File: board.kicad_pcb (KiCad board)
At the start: 4 copper layers, 90 x 80 mm, 13 parts, among them J1 chip_inst_mem_o, J10 chip_data_mem_o_1, J11 base, J12 power, J2 chip_data_mem_o_1, J3 data_mem_i, J4 chip_data_mem_o_1, J5 data_mem_i, J6 chip_data_mem_o_3, J7 inst_mem_i, J8 inst_mem_i, J9 chip_data_mem_o_1, U1 BERYL-MBLite

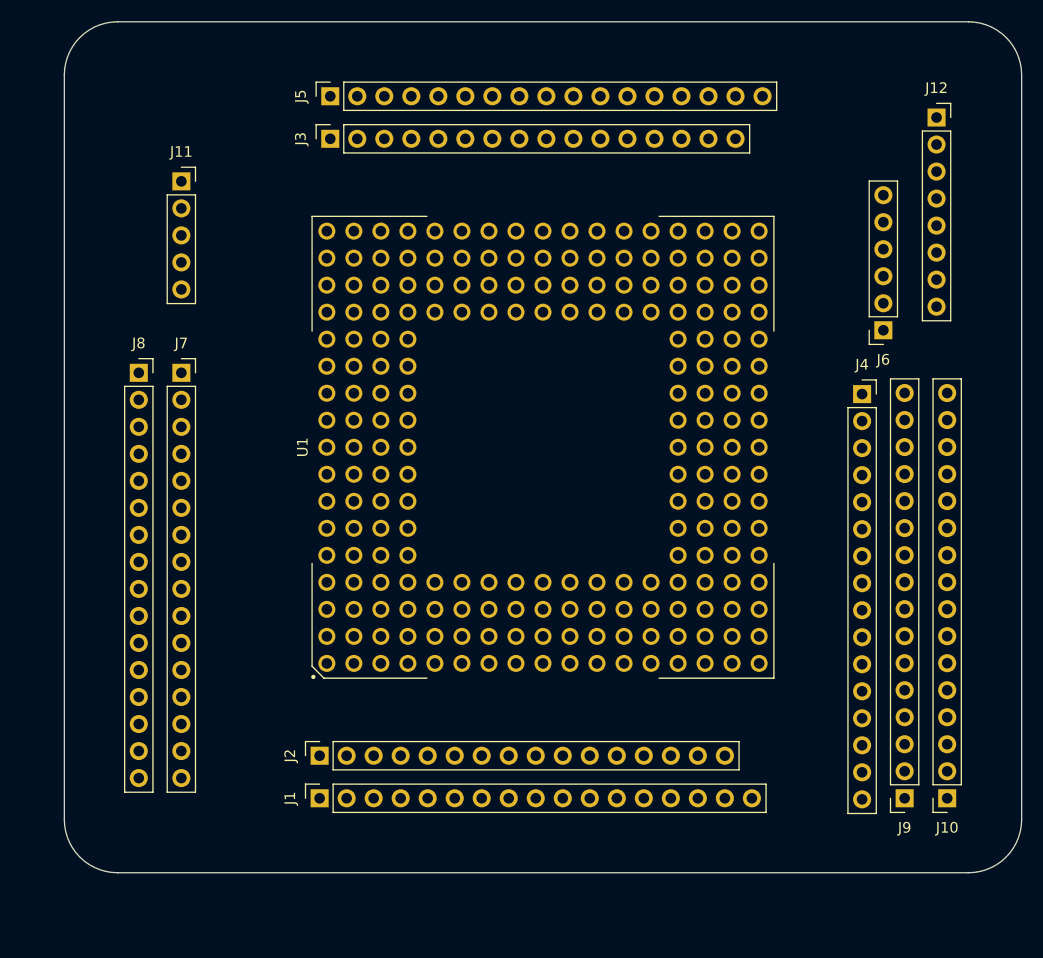
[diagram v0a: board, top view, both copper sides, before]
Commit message: Change headers to SMD and add decoupling capacitors
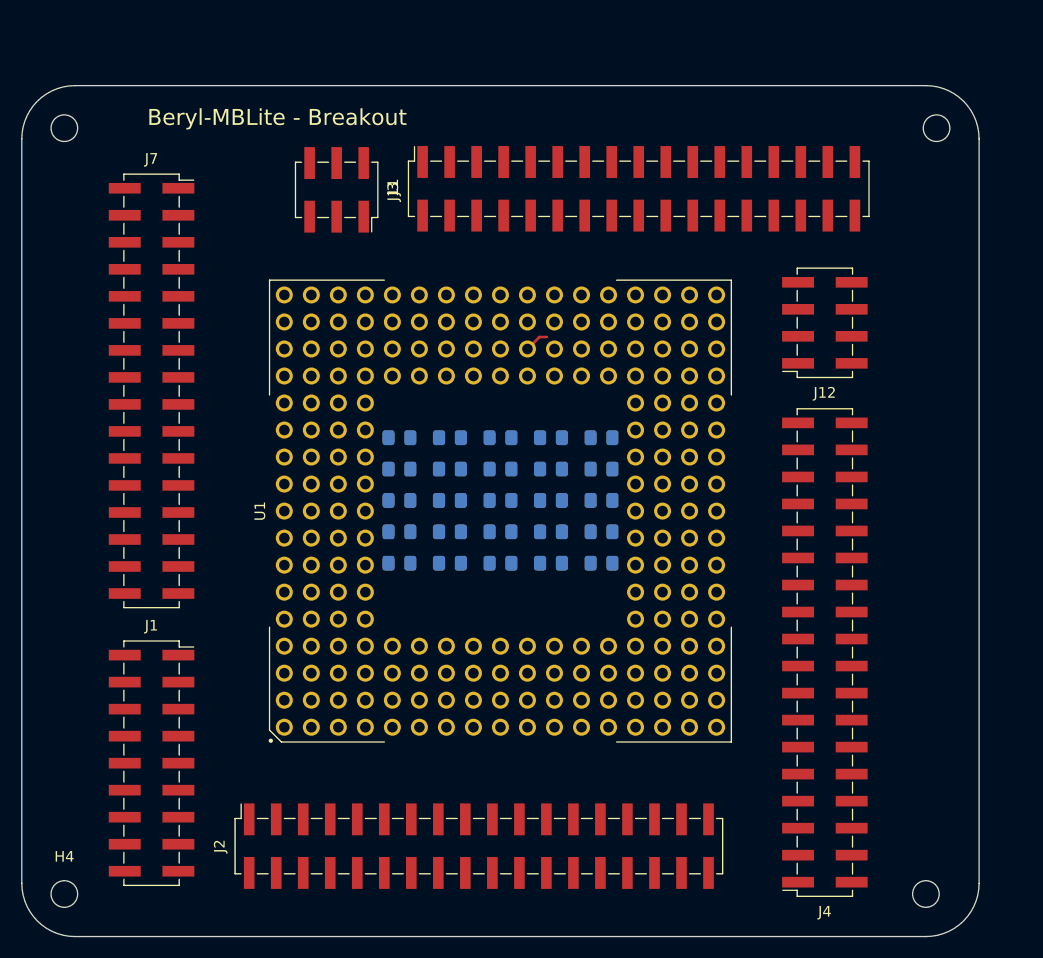
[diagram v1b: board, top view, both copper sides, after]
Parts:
- removed J10, J9: chip_data_mem_o_1, Connector_PinSocket_2.54mm:PinSocket_1x16_P2.54mm_Vertical
- removed J5: data_mem_i, Connector_PinSocket_2.54mm:PinSocket_1x17_P2.54mm_Vertical
- removed J6: chip_data_mem_o_3, Connector_PinSocket_2.54mm:PinSocket_1x06_P2.54mm_Vertical
- removed J8: inst_mem_i, Connector_PinSocket_2.54mm:PinSocket_1x16_P2.54mm_Vertical
- added C1: 100n, Capacitor_SMD:C_0805_2012Metric_Pad1.15x1.40mm_HandSolder, B.Cu at (151.0, 95.0)
- added C10: 100n, Capacitor_SMD:C_0805_2012Metric_Pad1.15x1.40mm_HandSolder, B.Cu at (141.5, 89.1)
- added C11: 100n, Capacitor_SMD:C_0805_2012Metric_Pad1.15x1.40mm_HandSolder, B.Cu at (155.8, 100.9)
- added C12: 100n, Capacitor_SMD:C_0805_2012Metric_Pad1.15x1.40mm_HandSolder, B.Cu at (146.2, 92.0)
- added C13: 100n, Capacitor_SMD:C_0805_2012Metric_Pad1.15x1.40mm_HandSolder, B.Cu at (155.8, 98.0)
- added C14: 100n, Capacitor_SMD:C_0805_2012Metric_Pad1.15x1.40mm_HandSolder, B.Cu at (141.5, 100.9)
- added C15: 100n, Capacitor_SMD:C_0805_2012Metric_Pad1.15x1.40mm_HandSolder, B.Cu at (146.2, 89.1)
- added C16: 100n, Capacitor_SMD:C_0805_2012Metric_Pad1.15x1.40mm_HandSolder, B.Cu at (160.5, 100.9)
- added C17: 100n, Capacitor_SMD:C_0805_2012Metric_Pad1.15x1.40mm_HandSolder, B.Cu at (151.0, 92.0)
- added C18: 100n, Capacitor_SMD:C_0805_2012Metric_Pad1.15x1.40mm_HandSolder, B.Cu at (155.8, 95.0)
- added C19: 100n, Capacitor_SMD:C_0805_2012Metric_Pad1.15x1.40mm_HandSolder, B.Cu at (160.5, 98.0)
- added C2: 100n, Capacitor_SMD:C_0805_2012Metric_Pad1.15x1.40mm_HandSolder, B.Cu at (141.5, 98.0)
- added C20: 100n, Capacitor_SMD:C_0805_2012Metric_Pad1.15x1.40mm_HandSolder, B.Cu at (151.0, 89.1)
- added C21: 100n, Capacitor_SMD:C_0805_2012Metric_Pad1.15x1.40mm_HandSolder, B.Cu at (155.8, 92.0)
- added C22: 100n, Capacitor_SMD:C_0805_2012Metric_Pad1.15x1.40mm_HandSolder, B.Cu at (160.5, 95.0)
- added C23: 100n, Capacitor_SMD:C_0805_2012Metric_Pad1.15x1.40mm_HandSolder, B.Cu at (155.8, 89.1)
- added C24: 100n, Capacitor_SMD:C_0805_2012Metric_Pad1.15x1.40mm_HandSolder, B.Cu at (160.5, 92.0)
- added C25: 100n, Capacitor_SMD:C_0805_2012Metric_Pad1.15x1.40mm_HandSolder, B.Cu at (160.5, 89.1)
- added C3: 100n, Capacitor_SMD:C_0805_2012Metric_Pad1.15x1.40mm_HandSolder, B.Cu at (146.2, 100.9)
- added C4: 100n, Capacitor_SMD:C_0805_2012Metric_Pad1.15x1.40mm_HandSolder, B.Cu at (141.5, 95.0)
- added C5: 100n, Capacitor_SMD:C_0805_2012Metric_Pad1.15x1.40mm_HandSolder, B.Cu at (146.2, 98.0)
- added C6: 100n, Capacitor_SMD:C_0805_2012Metric_Pad1.15x1.40mm_HandSolder, B.Cu at (151.0, 100.9)
- added C7: 100n, Capacitor_SMD:C_0805_2012Metric_Pad1.15x1.40mm_HandSolder, B.Cu at (141.5, 92.0)
- added C8: 100n, Capacitor_SMD:C_0805_2012Metric_Pad1.15x1.40mm_HandSolder, B.Cu at (146.2, 95.0)
- added C9: 100n, Capacitor_SMD:C_0805_2012Metric_Pad1.15x1.40mm_HandSolder, B.Cu at (151.0, 98.0)
- added H1: MountingHole, MountingHole:MountingHole_2.5mm, F.Cu at (110.0, 60.0)
- added H2: MountingHole, MountingHole:MountingHole_2.5mm, F.Cu at (192.0, 60.0)
- added H3: MountingHole, MountingHole:MountingHole_2.5mm, F.Cu at (191.0, 132.0)
- added H4: MountingHole, MountingHole:MountingHole_2.5mm, F.Cu at (110.0, 132.0)
- J1: footprint Connector_PinSocket_2.54mm:PinSocket_1x17_P2.54mm_Vertical -> Connector_PinSocket_2.54mm:PinSocket_2x09_P2.54mm_Vertical_SMD
- J11: footprint Connector_PinSocket_2.54mm:PinSocket_1x05_P2.54mm_Vertical -> Connector_PinSocket_2.54mm:PinSocket_2x03_P2.54mm_Vertical_SMD
- J12: footprint Connector_PinSocket_2.54mm:PinSocket_1x08_P2.54mm_Vertical -> Connector_PinSocket_2.54mm:PinSocket_2x04_P2.54mm_Vertical_SMD
- J2, J4: footprint Connector_PinSocket_2.54mm:PinSocket_1x16_P2.54mm_Vertical -> Connector_PinSocket_2.54mm:PinSocket_2x18_P2.54mm_Vertical_SMD
- J3: footprint Connector_PinSocket_2.54mm:PinSocket_1x16_P2.54mm_Vertical -> Connector_PinSocket_2.54mm:PinSocket_2x17_P2.54mm_Vertical_SMD
- J7: footprint Connector_PinSocket_2.54mm:PinSocket_1x16_P2.54mm_Vertical -> Connector_PinSocket_2.54mm:PinSocket_2x16_P2.54mm_Vertical_SMD
- moved J3 29.4 mm to (164.0, 65.7)
- moved J4 24.6 mm to (181.5, 109.3), turned to 180 degrees
- moved J12 22.0 mm to (181.5, 78.3), turned to 180 degrees
- moved J2 17.2 mm to (149.0, 127.5)
- moved J1 16.1 mm to (118.2, 119.7), turned to 0 degrees
- moved J11 14.6 mm to (135.6, 65.8), turned to 270 degrees
- moved U1 7.21 mm to (151.0, 96.0)
- moved J7 3.28 mm to (118.2, 84.7)
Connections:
- U1 pad 1: Net-(J8-Pad7) -> Net-(J7-Pad10)
- U1 pad 10: Net-(J7-Pad1) -> Net-(J7-Pad17)
- U1 pad 100: Net-(J4-Pad5) -> Net-(J2-Pad21)
- U1 pad 101: Net-(J4-Pad4) -> Net-(J2-Pad20)
- U1 pad 102: Net-(J4-Pad3) -> Net-(J2-Pad19)
- U1 pad 103: Net-(J4-Pad2) -> Net-(J2-Pad18)
- U1 pad 104: Net-(J4-Pad1) -> Net-(J2-Pad17)
- U1 pad 107: Net-(J9-Pad5) -> Net-(J4-Pad2)
- U1 pad 108: Net-(J9-Pad6) -> Net-(J4-Pad3)
- U1 pad 109: Net-(J9-Pad7) -> Net-(J4-Pad4)
- U1 pad 11: Net-(J7-Pad2) -> Net-(J7-Pad18)
- U1 pad 110: Net-(J9-Pad8) -> Net-(J4-Pad5)
- U1 pad 111: Net-(J9-Pad9) -> Net-(J4-Pad6)
- U1 pad 112: Net-(J9-Pad10) -> Net-(J4-Pad7)
- U1 pad 113: Net-(J9-Pad11) -> Net-(J4-Pad8)
- U1 pad 114: Net-(J9-Pad12) -> Net-(J4-Pad9)
- U1 pad 115: Net-(J9-Pad13) -> Net-(J4-Pad10)
- U1 pad 118: Net-(J9-Pad14) -> Net-(J4-Pad11)
- U1 pad 119: Net-(J9-Pad15) -> Net-(J4-Pad12)
- U1 pad 12: Net-(J7-Pad3) -> Net-(J7-Pad19)
- U1 pad 122: Net-(J9-Pad16) -> Net-(J4-Pad13)
- U1 pad 123: Net-(J10-Pad1) -> Net-(J4-Pad14)
- U1 pad 124: Net-(J10-Pad2) -> Net-(J4-Pad15)
- U1 pad 125: Net-(J10-Pad3) -> Net-(J4-Pad16)
- U1 pad 126: Net-(J10-Pad4) -> Net-(J4-Pad17)
- U1 pad 127: Net-(J10-Pad5) -> Net-(J4-Pad18)
- U1 pad 128: Net-(J10-Pad6) -> Net-(J4-Pad19)
- U1 pad 129: Net-(J10-Pad7) -> Net-(J4-Pad20)
- U1 pad 13: Net-(J7-Pad4) -> Net-(J7-Pad20)
- U1 pad 130: Net-(J10-Pad8) -> Net-(J4-Pad21)
- U1 pad 131: Net-(J10-Pad9) -> Net-(J4-Pad22)
- U1 pad 132: Net-(J10-Pad10) -> Net-(J4-Pad23)
- U1 pad 133: Net-(J10-Pad11) -> Net-(J4-Pad24)
- U1 pad 136: Net-(J10-Pad12) -> Net-(J4-Pad25)
- U1 pad 139: Net-(J10-Pad13) -> Net-(J4-Pad26)
- U1 pad 14: Net-(J7-Pad5) -> Net-(J7-Pad21)
- U1 pad 140: Net-(J10-Pad14) -> Net-(J4-Pad27)
- U1 pad 141: Net-(J10-Pad15) -> Net-(J4-Pad28)
- U1 pad 142: Net-(J10-Pad16) -> Net-(J4-Pad29)
- U1 pad 143: Net-(J6-Pad1) -> Net-(J4-Pad30)
- U1 pad 144: Net-(J6-Pad2) -> Net-(J4-Pad31)
- U1 pad 145: Net-(J6-Pad3) -> Net-(J4-Pad32)
- U1 pad 146: Net-(J6-Pad4) -> Net-(J4-Pad33)
- U1 pad 147: Net-(J6-Pad5) -> Net-(J4-Pad34)
- U1 pad 148: Net-(J6-Pad6) -> Net-(J4-Pad35)
- U1 pad 15: Net-(J7-Pad6) -> Net-(J7-Pad22)
- U1 pad 153: Net-(J5-Pad17) -> Net-(J3-Pad33)
- U1 pad 154: Net-(J5-Pad16) -> Net-(J3-Pad32)
- U1 pad 155: Net-(J5-Pad15) -> Net-(J3-Pad31)
- U1 pad 156: Net-(J5-Pad14) -> Net-(J3-Pad30)
- U1 pad 157: Net-(J5-Pad13) -> Net-(J3-Pad29)
- U1 pad 158: Net-(J5-Pad12) -> Net-(J3-Pad28)
- U1 pad 159: Net-(J5-Pad11) -> Net-(J3-Pad27)
- U1 pad 160: Net-(J5-Pad10) -> Net-(J3-Pad26)
- U1 pad 163: Net-(J5-Pad9) -> Net-(J3-Pad25)
- U1 pad 164: Net-(J5-Pad8) -> Net-(J3-Pad24)
- U1 pad 165: Net-(J5-Pad7) -> Net-(J3-Pad23)
- U1 pad 166: Net-(J5-Pad6) -> Net-(J3-Pad22)
- U1 pad 167: Net-(J5-Pad5) -> Net-(J3-Pad21)
- U1 pad 168: Net-(J5-Pad4) -> Net-(J3-Pad20)
- U1 pad 169: Net-(J5-Pad3) -> Net-(J3-Pad19)
- U1 pad 170: Net-(J5-Pad2) -> Net-(J3-Pad18)
- U1 pad 171: Net-(J5-Pad1) -> Net-(J3-Pad17)
- U1 pad 18: Net-(J7-Pad7) -> Net-(J7-Pad23)
- U1 pad 19: Net-(J7-Pad8) -> Net-(J7-Pad24)
- U1 pad 192: Net-(J8-Pad16) -> Net-(J7-Pad1)
- U1 pad 193: Net-(J8-Pad15) -> Net-(J7-Pad2)
- U1 pad 2: Net-(J8-Pad6) -> Net-(J7-Pad11)
- U1 pad 20: Net-(J7-Pad9) -> Net-(J7-Pad25)
- U1 pad 202: Net-(J8-Pad14) -> Net-(J7-Pad3)
- U1 pad 203: Net-(J8-Pad13) -> Net-(J7-Pad4)
- U1 pad 204: Net-(J8-Pad12) -> Net-(J7-Pad5)
- U1 pad 205: Net-(J8-Pad11) -> Net-(J7-Pad6)
- U1 pad 206: Net-(J8-Pad10) -> Net-(J7-Pad7)
- U1 pad 207: Net-(J8-Pad9) -> Net-(J7-Pad8)
- U1 pad 208: Net-(J8-Pad8) -> Net-(J7-Pad9)
- U1 pad 21: Net-(J7-Pad10) -> Net-(J7-Pad26)
- U1 pad 22: Net-(J7-Pad11) -> Net-(J7-Pad27)
- U1 pad 23: Net-(J7-Pad12) -> Net-(J7-Pad28)
- U1 pad 24: Net-(J7-Pad13) -> Net-(J7-Pad29)
- U1 pad 27: Net-(J7-Pad14) -> Net-(J7-Pad30)
- U1 pad 28: Net-(J7-Pad15) -> Net-(J7-Pad31)
- U1 pad 29: Net-(J7-Pad16) -> Net-(J7-Pad32)
- U1 pad 3: Net-(J8-Pad5) -> Net-(J7-Pad12)
- U1 pad 4: Net-(J8-Pad4) -> Net-(J7-Pad13)
- U1 pad 5: Net-(J8-Pad3) -> Net-(J7-Pad14)
- U1 pad 6: Net-(J8-Pad2) -> Net-(J7-Pad15)
- U1 pad 7: Net-(J8-Pad1) -> Net-(J7-Pad16)
- U1 pad 79: Net-(J9-Pad4) -> Net-(J4-Pad1)
- U1 pad 80: Net-(J9-Pad3) -> Net-(J2-Pad35)
- U1 pad 81: Net-(J9-Pad2) -> Net-(J2-Pad34)
- U1 pad 82: Net-(J9-Pad1) -> Net-(J2-Pad33)
- U1 pad 83: Net-(J4-Pad16) -> Net-(J2-Pad32)
- U1 pad 84: Net-(J4-Pad15) -> Net-(J2-Pad31)
- U1 pad 85: Net-(J4-Pad14) -> Net-(J2-Pad30)
- U1 pad 88: Net-(J4-Pad13) -> Net-(J2-Pad29)
- U1 pad 89: Net-(J4-Pad12) -> Net-(J2-Pad28)
- U1 pad 90: Net-(J4-Pad11) -> Net-(J2-Pad27)
- U1 pad 93: Net-(J4-Pad10) -> Net-(J2-Pad26)
- U1 pad 94: Net-(J4-Pad9) -> Net-(J2-Pad25)
- U1 pad 95: Net-(J4-Pad8) -> Net-(J2-Pad24)
- U1 pad 96: Net-(J4-Pad7) -> Net-(J2-Pad23)
- U1 pad 99: Net-(J4-Pad6) -> Net-(J2-Pad22)
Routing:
- net +1V8: track 0.00 -> 154.9 mm
- net +3V3: track 0.00 -> 133.3 mm
- net GND: track 0.00 -> 7.62 mm
- net Net-(J3-Pad12): track 0.00 -> 2.29 mm
- net Net-(J3-Pad14): track 0.00 -> 0.69 mm
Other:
- board text added: "Beryl-MBLite - Breakout"
- board text added: "Grupo de Apoio ao Projeto de Hardware GAPH - PUCRS - xx.xx.xx"

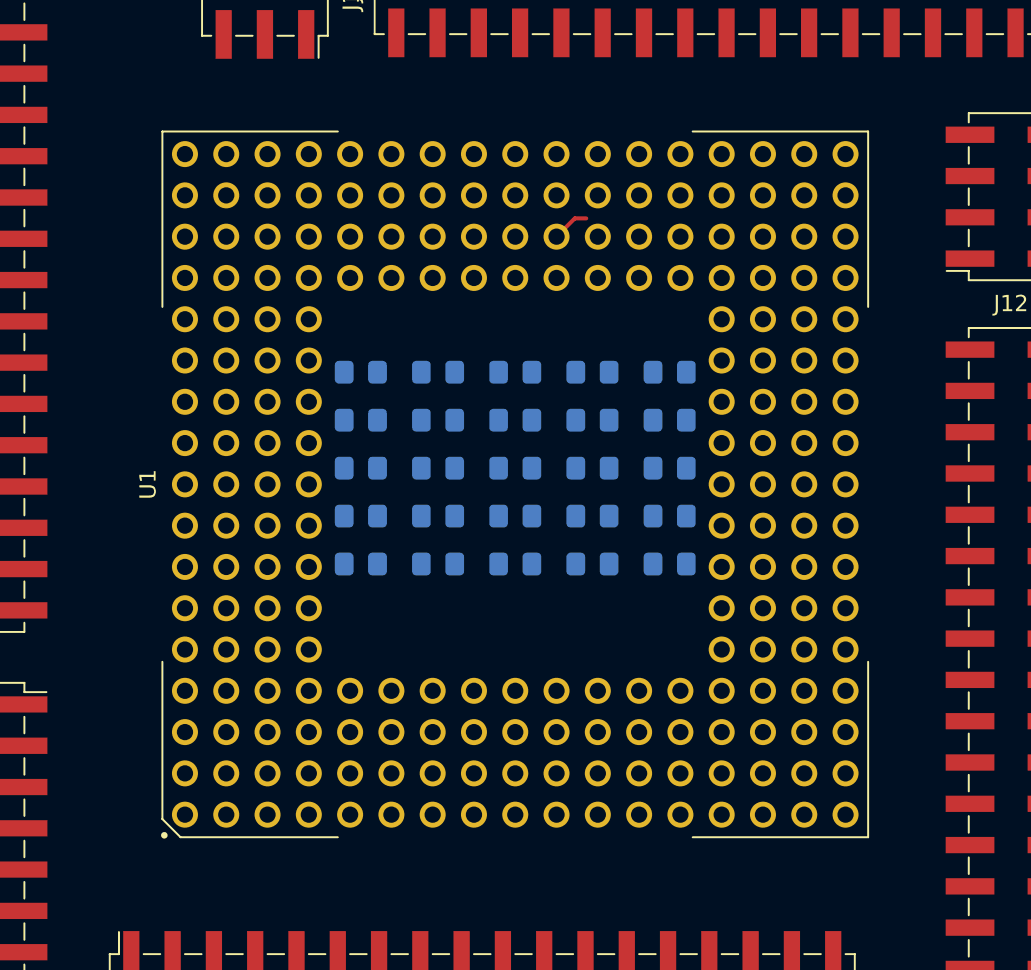
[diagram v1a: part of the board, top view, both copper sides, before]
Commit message: Improve capacitors placement
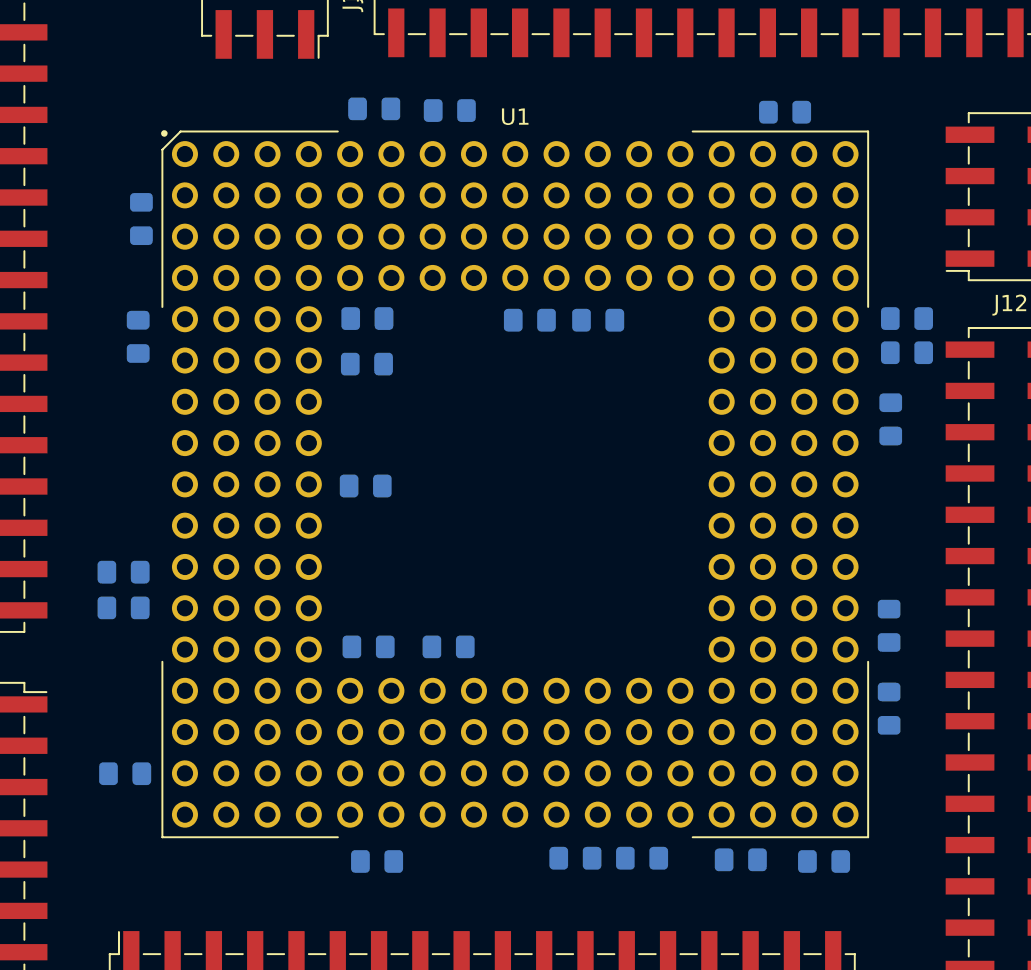
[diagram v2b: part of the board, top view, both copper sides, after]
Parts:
- J11: value base -> Main
- moved C16 35.6 mm to (127.8, 86.9), turned to 270 degrees
- moved C18 34.4 mm to (127.0, 113.8), turned to 180 degrees
- moved C10 33.8 mm to (175.1, 85.8)
- moved C20 30.9 mm to (158.8, 119.0)
- moved C11 30.2 mm to (167.6, 73.1)
- moved C21 28.5 mm to (164.9, 119.1)
- moved C9 28.5 mm to (170.0, 119.2)
- moved C14 28.0 mm to (142.3, 72.9), turned to 180 degrees
- moved C19 27.8 mm to (142.5, 119.2), turned to 180 degrees
- moved C17 25.9 mm to (126.9, 101.4), turned to 180 degrees
- moved C8 25.4 mm to (154.7, 119.0)
- moved C23 24.0 mm to (174.0, 104.7), turned to 270 degrees
- moved C1 22.4 mm to (147.0, 73.0)
- moved C15 20.5 mm to (128.0, 79.7), turned to 90 degrees
- moved C5 20.2 mm to (126.9, 103.6), turned to 180 degrees
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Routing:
- net +1V8: track 154.9 -> 0.00 mm
- net +3V3: track 133.3 -> 0.00 mm
- net GND: track 7.62 -> 0.00 mm
- net Net-(J3-Pad12): track 2.29 -> 0.00 mm
- net Net-(J3-Pad14): track 0.69 -> 0.00 mm

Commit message: Update info
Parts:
- moved C8 3.50 mm to (151.2, 118.9), turned to 180 degrees
- moved J1 2.78 mm to (116.5, 117.5)
- moved J2 2.22 mm to (150.6, 129.0)
- moved J7 2.13 mm to (116.6, 83.3)
- moved J4 2.02 mm to (183.2, 108.2)
- moved C20 1.80 mm to (157.0, 119.0)
- moved J12 1.68 mm to (183.1, 77.8)
- moved J11 1.61 mm to (137.0, 65.0)
- moved J3 1.61 mm to (165.4, 64.9)
- moved C21 1.48 mm to (163.4, 119.0)
- moved C18 1.45 mm to (128.0, 114.8), turned to 270 degrees
- moved C19 1.43 mm to (141.1, 118.9)
- moved C5 1.41 mm to (127.9, 104.6), turned to 90 degrees
- moved C17 1.28 mm to (127.9, 100.6), turned to 270 degrees
- moved C15 1.28 mm to (127.9, 78.4)
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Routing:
- net +1V8: track 0.00 -> 71.3 mm
- net GND: track 0.00 -> 39.9 mm, vias 0 -> 23
- net +3V3: track 0.00 -> 34.6 mm
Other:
- board text added: "Grupo de Apoio ao Projeto de Hardware GAPH - PUCRS - March 2014"
- board text removed: "Grupo de Apoio ao Projeto de Hardware GAPH - PUCRS - xx.xx.xx"
